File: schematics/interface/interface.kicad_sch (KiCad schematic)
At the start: 27 parts, among them U1 74LS00, U2 74LS00, U4 74LS245, U5 74LS193, U6 74LS193, U7 74LS193, U8 74LS193

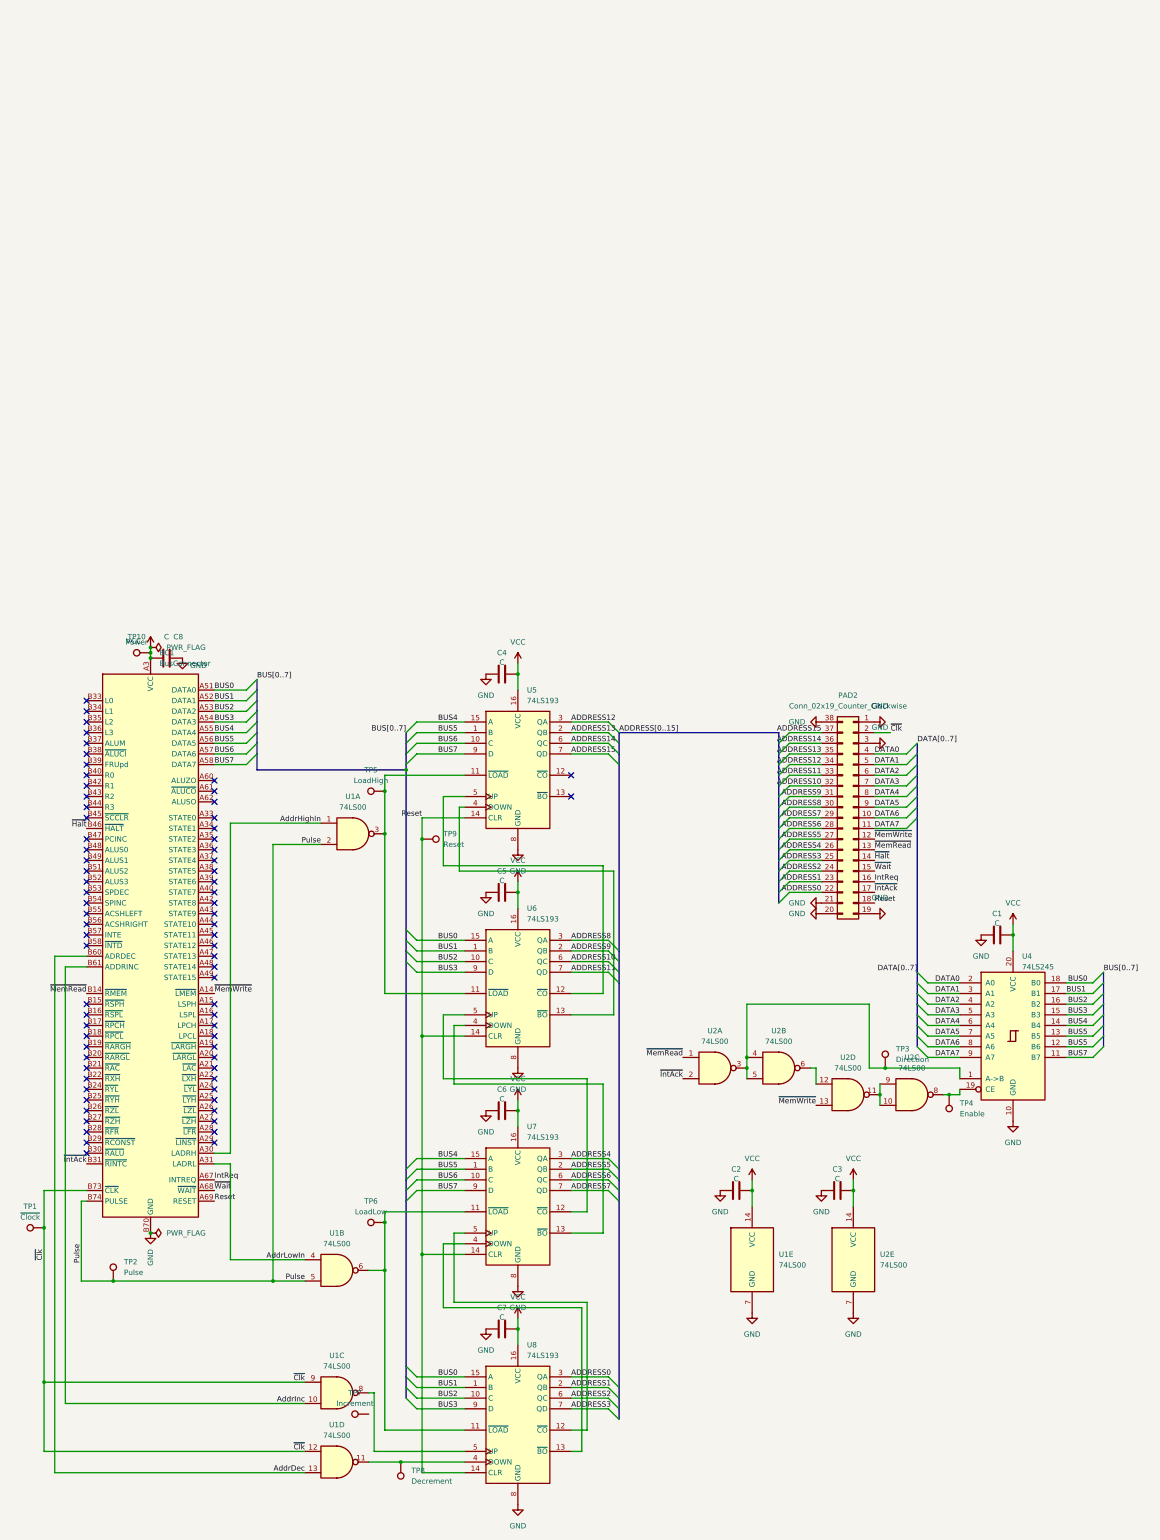
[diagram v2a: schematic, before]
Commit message: fix(alu, interface): fix tp
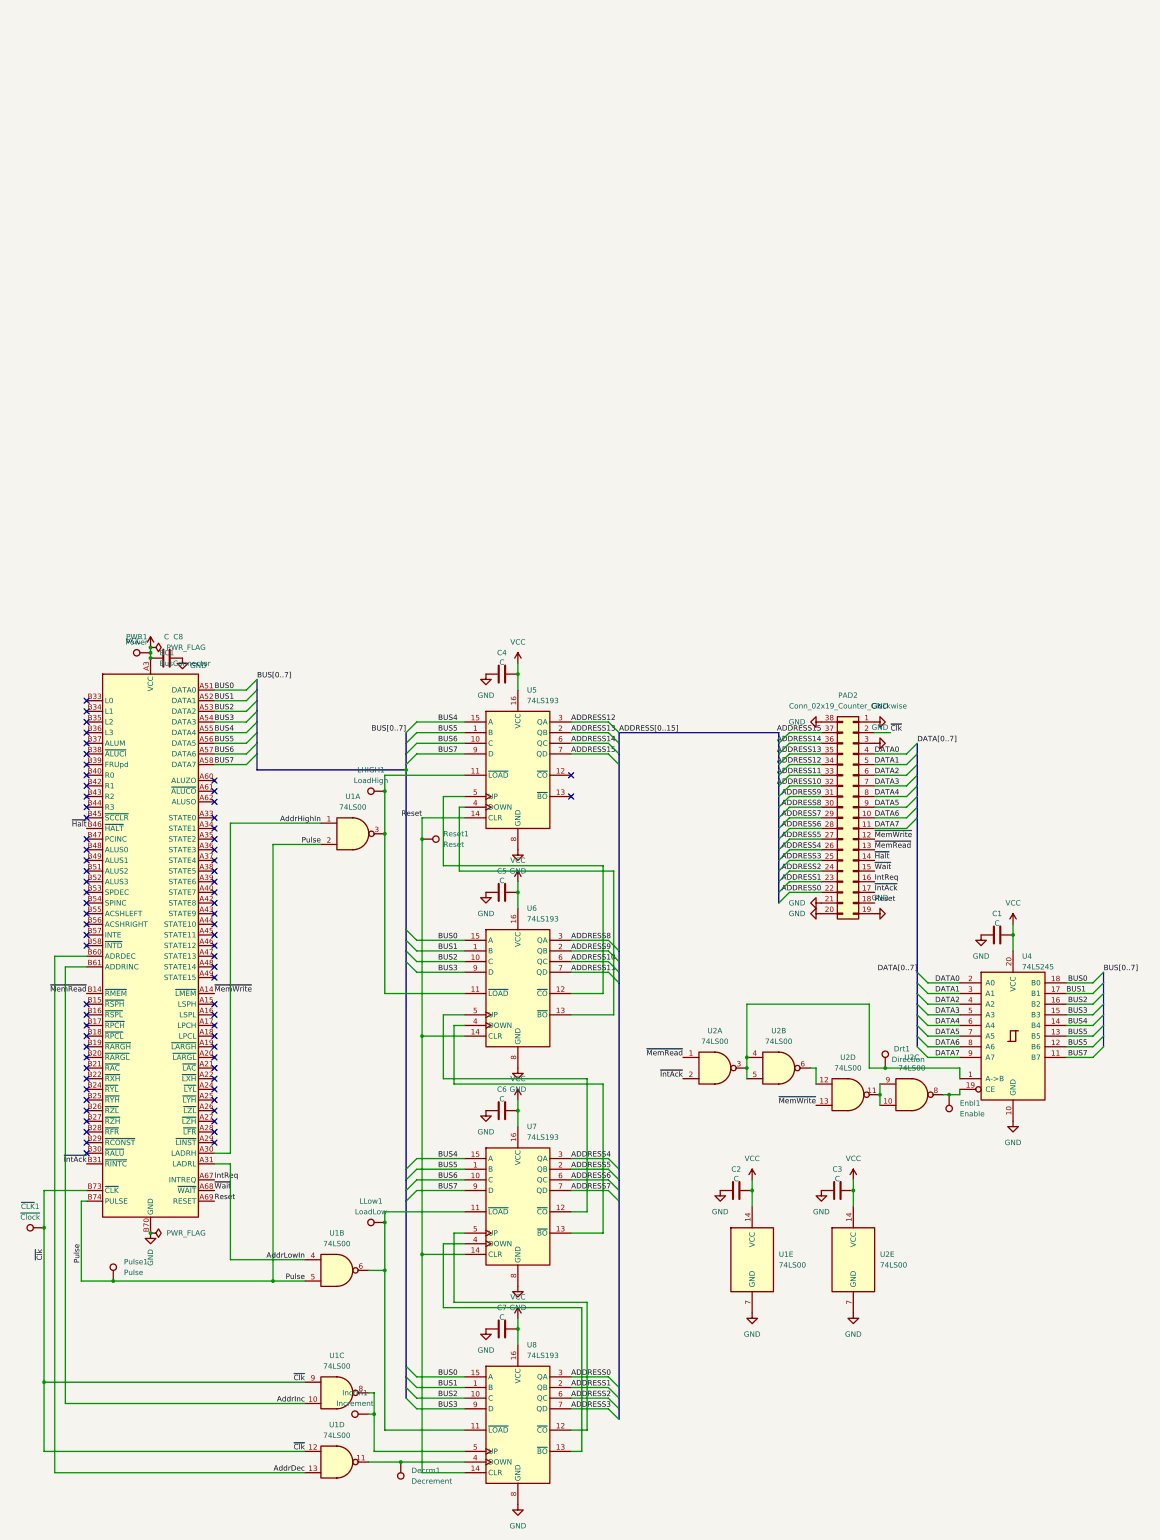
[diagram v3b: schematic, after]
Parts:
- Decrm1: renamed from TP8; footprint Connector_Pin:Pin_D1.0mm_L10.0mm -> TestPoint:TestPoint_Pad_D1.0mm
- Drt1: renamed from TP3; footprint Connector_Pin:Pin_D1.0mm_L10.0mm -> TestPoint:TestPoint_Pad_D1.0mm
- Enbl1: renamed from TP4; footprint Connector_Pin:Pin_D1.0mm_L10.0mm -> TestPoint:TestPoint_Pad_D1.0mm
- Incrm1: renamed from TP7; footprint Connector_Pin:Pin_D1.0mm_L10.0mm -> TestPoint:TestPoint_Pad_D1.0mm
- LHIGH1: renamed from TP5; footprint Connector_Pin:Pin_D1.0mm_L10.0mm -> TestPoint:TestPoint_Pad_D1.0mm
- LLow1: renamed from TP6; footprint Connector_Pin:Pin_D1.0mm_L10.0mm -> TestPoint:TestPoint_Pad_D1.0mm
- PWR1: renamed from TP10; footprint Connector_Pin:Pin_D1.0mm_L10.0mm -> TestPoint:TestPoint_Pad_D1.0mm
- Pulse1: renamed from TP2; footprint Connector_Pin:Pin_D1.0mm_L10.0mm -> TestPoint:TestPoint_Pad_D1.0mm
- Reset1: renamed from TP9; footprint Connector_Pin:Pin_D1.0mm_L10.0mm -> TestPoint:TestPoint_Pad_D1.0mm
- ~{CLK}1: renamed from TP1; footprint Connector_Pin:Pin_D1.0mm_L10.0mm -> TestPoint:TestPoint_Pad_D1.0mm
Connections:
- net at U1.8, U8.5 (UP): now also Incrm1.1
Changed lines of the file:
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@@
 	)
 	(junction
+		(at 106.68 184.15)
+		(diameter 0)
+		(color 0 0 0 0)
+	)
+	(junction
 		(at 109.22 35.56)
 		(diameter 0)
@@
 	(wire
 		(pts
-			(xy 106.68 179.07) (xy 106.68 193.04)
+			(xy 106.68 179.07) (xy 106.68 184.15)
 		)
 		(stroke
@@
 		)
 	)
+	(wire
+		(pts
+			(xy 105.41 184.15) (xy 106.68 184.15)
+		)
+		(stroke
+			(width 0)
+			(type default)
+		)
+	)
 	(bus
 		(pts
@@
 	(wire
 		(pts
+			(xy 106.68 184.15) (xy 106.68 193.04)
+		)
+		(stroke
+			(width 0)
+			(type default)
+		)
+	)
+	(wire
+		(pts
 			(xy 246.38 93.98) (xy 238.76 93.98)
 		)
@@
 		(dnp no)
 		(fields_autoplaced yes)
-		(property "Reference" "TP6"
+		(property "Reference" "LLow1"
 			(at 105.918 133.35 90)
 			(effects
@@
 			)
 		)
-		(property "Footprint" "Connector_Pin:Pin_D1.0mm_L10.0mm"
+		(property "Footprint" "TestPoint:TestPoint_Pad_D1.0mm"
 			(at 109.22 133.35 0)
 			(effects
@@
 			(project "interface"
 				(path "/a2b820ea-2fb5-45d1-b9ac-854bc1de3ffd"
-					(reference "TP6")
+					(reference "LLow1")
 					(unit 1)
 				)
@@
 		(on_board yes)
 		(dnp no)
-		(fields_autoplaced yes)
-		(property "Reference" "TP3"
-			(at 231.14 97.0279 0)
+		(property "Reference" "Drt1"
+			(at 230.632 97.028 0)
 			(effects
 				(font
@@
 		)
 		(property "Value" "Direction"
-			(at 231.14 99.5679 0)
+			(at 230.124 99.568 0)
 			(effects
 				(font
@@
 			)
 		)
-		(property "Footprint" "Connector_Pin:Pin_D1.0mm_L10.0mm"
+		(property "Footprint" "TestPoint:TestPoint_Pad_D1.0mm"
 			(at 233.68 101.6 0)
 			(effects
@@
 			(project "interface"
 				(path "/a2b820ea-2fb5-45d1-b9ac-854bc1de3ffd"
-					(reference "TP3")
+					(reference "Drt1")
 					(unit 1)
 				)
@@
 		(dnp no)
 		(fields_autoplaced yes)
-		(property "Reference" "TP2"
+		(property "Reference" "Pulse1"
 			(at 46.99 147.8279 0)
 			(effects
@@
 			)
 		)
-		(property "Footprint" "Connector_Pin:Pin_D1.0mm_L10.0mm"
+		(property "Footprint" "TestPoint:TestPoint_Pad_D1.0mm"
 			(at 49.53 152.4 0)
 			(effects
@@
 			(project "interface"
 				(path "/a2b820ea-2fb5-45d1-b9ac-854bc1de3ffd"
-					(reference "TP2")
+					(reference "Pulse1")
 					(unit 1)
 				)
@@
 		(dnp no)
 		(fields_autoplaced yes)
-		(property "Reference" "TP5"
+		(property "Reference" "LHIGH1"
 			(at 105.918 30.48 90)
 			(effects
@@
 			)
 		)
-		(property "Footprint" "Connector_Pin:Pin_D1.0mm_L10.0mm"
+		(property "Footprint" "TestPoint:TestPoint_Pad_D1.0mm"
 			(at 109.22 30.48 0)
 			(effects
@@
 			(project "interface"
 				(path "/a2b820ea-2fb5-45d1-b9ac-854bc1de3ffd"
-					(reference "TP5")
+					(reference "LHIGH1")
 					(unit 1)
 				)
@@
 		(dnp no)
 		(fields_autoplaced yes)
-		(property "Reference" "TP8"
+		(property "Reference" "Decrm1"
 			(at 115.57 197.6119 0)
 			(effects
@@
 			)
 		)
-		(property "Footprint" "Connector_Pin:Pin_D1.0mm_L10.0mm"
+		(property "Footprint" "TestPoint:TestPoint_Pad_D1.0mm"
 			(at 107.95 195.58 0)
 			(effects
@@
 			(project "interface"
 				(path "/a2b820ea-2fb5-45d1-b9ac-854bc1de3ffd"
-					(reference "TP8")
+					(reference "Decrm1")
 					(unit 1)
 				)
@@
 		(dnp no)
 		(fields_autoplaced yes)
-		(property "Reference" "TP7"
+		(property "Reference" "Incrm1"
 			(at 102.108 179.07 90)
 			(effects
@@
 			)
 		)
-		(property "Footprint" "Connector_Pin:Pin_D1.0mm_L10.0mm"
+		(property "Footprint" "TestPoint:TestPoint_Pad_D1.0mm"
 			(at 105.41 179.07 0)
 			(effects
@@
 			(project "interface"
 				(path "/a2b820ea-2fb5-45d1-b9ac-854bc1de3ffd"
-					(reference "TP7")
+					(reference "Incrm1")
 					(unit 1)
 				)
@@
 		(dnp no)
 		(fields_autoplaced yes)
-		(property "Reference" "TP9"
+		(property "Reference" "Reset1"
 			(at 123.19 45.7199 90)
 			(effects
@@
 			)
 		)
-		(property "Footprint" "Connector_Pin:Pin_D1.0mm_L10.0mm"
+		(property "Footprint" "TestPoint:TestPoint_Pad_D1.0mm"
 			(at 118.11 52.07 0)
 			(effects
@@
 			(project "interface"
 				(path "/a2b820ea-2fb5-45d1-b9ac-854bc1de3ffd"
-					(reference "TP9")
+					(reference "Reset1")
 					(unit 1)
 				)
@@
 		(dnp no)
 		(fields_autoplaced yes)
-		(property "Reference" "TP4"
+		(property "Reference" "Enbl1"
 			(at 246.38 109.9819 0)
 			(effects
@@
 			)
 		)
-		(property "Footprint" "Connector_Pin:Pin_D1.0mm_L10.0mm"
+		(property "Footprint" "TestPoint:TestPoint_Pad_D1.0mm"
 			(at 238.76 107.95 0)
 			(effects
@@
 			(project "interface"
 				(path "/a2b820ea-2fb5-45d1-b9ac-854bc1de3ffd"
-					(reference "TP4")
+					(reference "Enbl1")
 					(unit 1)
 				)
@@
 		(dnp no)
 		(fields_autoplaced yes)
-		(property "Reference" "TP10"
+		(property "Reference" "PWR1"
 			(at 50.038 -1.27 90)
 			(effects
@@
 			)
 		)
-		(property "Footprint" "Connector_Pin:Pin_D1.0mm_L10.0mm"
+		(property "Footprint" "TestPoint:TestPoint_Pad_D1.0mm"
 			(at 53.34 -2.54 0)
 			(effects
@@
 			(project "interface"
 				(path "/a2b820ea-2fb5-45d1-b9ac-854bc1de3ffd"
-					(reference "TP10")
+					(reference "PWR1")
 					(unit 1)
 				)
@@
 		(dnp no)
 		(fields_autoplaced yes)
-		(property "Reference" "TP1"
+		(property "Reference" "~{CLK}1"
 			(at 24.638 134.62 90)
 			(effects
@@
 			)
 		)
-		(property "Footprint" "Connector_Pin:Pin_D1.0mm_L10.0mm"
+		(property "Footprint" "TestPoint:TestPoint_Pad_D1.0mm"
 			(at 27.94 134.62 0)
 			(effects
@@
 			(project "interface"
 				(path "/a2b820ea-2fb5-45d1-b9ac-854bc1de3ffd"
-					(reference "TP1")
+					(reference "~{CLK}1")
 					(unit 1)
 				)

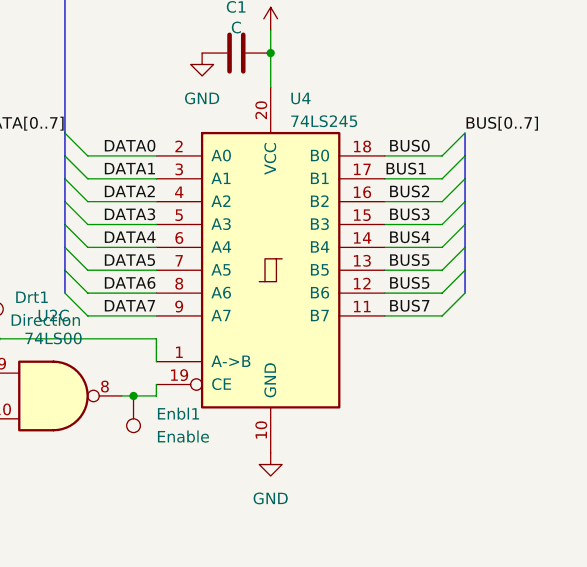
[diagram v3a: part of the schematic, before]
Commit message: Fix U4 connection in interface
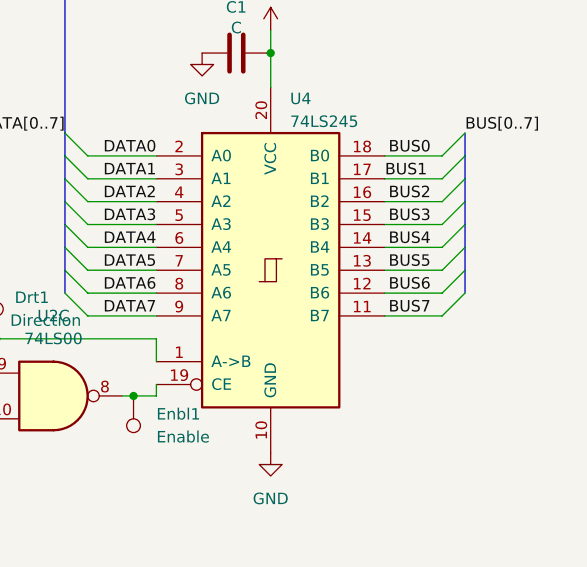
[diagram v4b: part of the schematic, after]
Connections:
- net BUS5: no longer U4.12 (B6)
- net BUS6: now also U4.12 (B6)
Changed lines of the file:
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@@
 		)
 	)
-	(label "BUS5"
+	(label "BUS6"
 		(at 276.86 96.52 180)
 		(effects
